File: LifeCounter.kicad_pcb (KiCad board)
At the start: 2 copper layers, 103 x 73 mm, 118 parts, among them J201 USBC, J701 Debug, Q201 2N7002, Q202 BSS84, Q801 2N7002, SW1 RotaryEncoder_Switch_MP, SW2 RotaryEncoder_Switch_MP, SW201 PWR_ON, SW701 RST, U1 74LVC3G14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

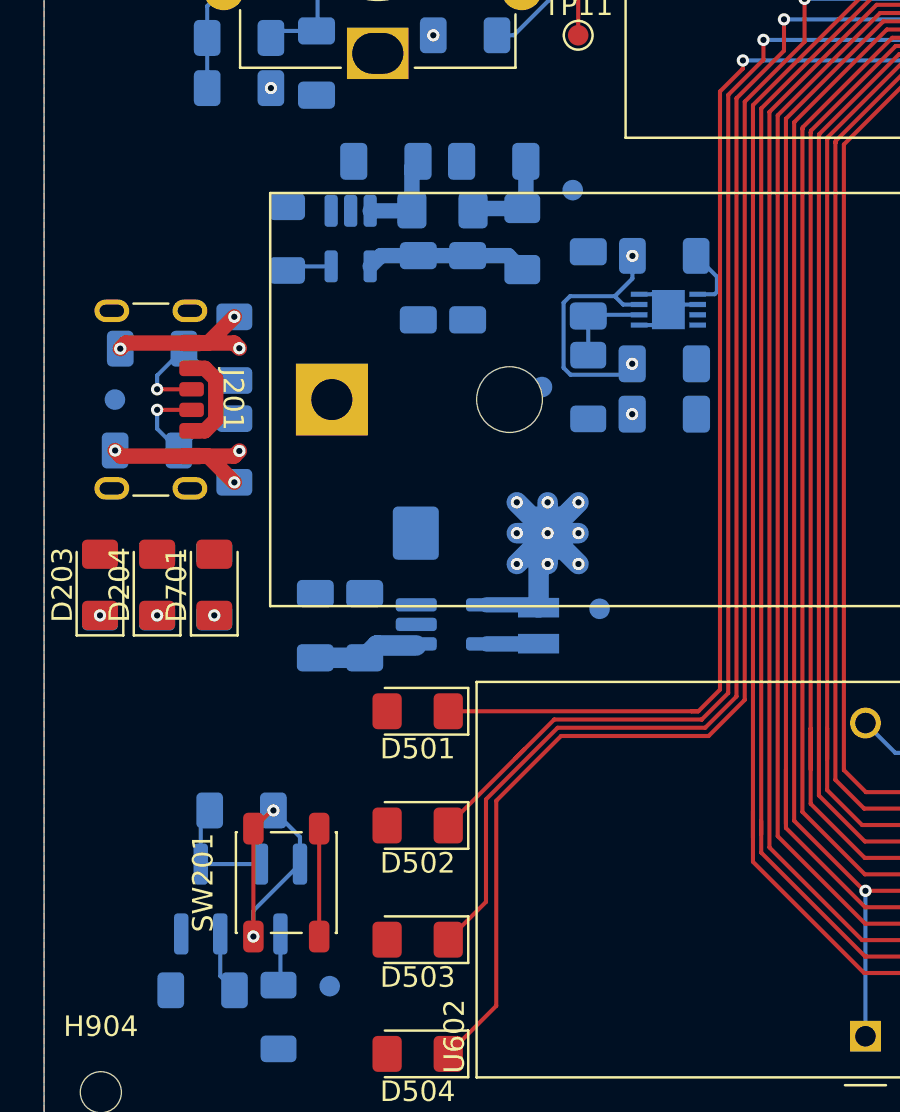
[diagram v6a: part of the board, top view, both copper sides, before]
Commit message: Power routed
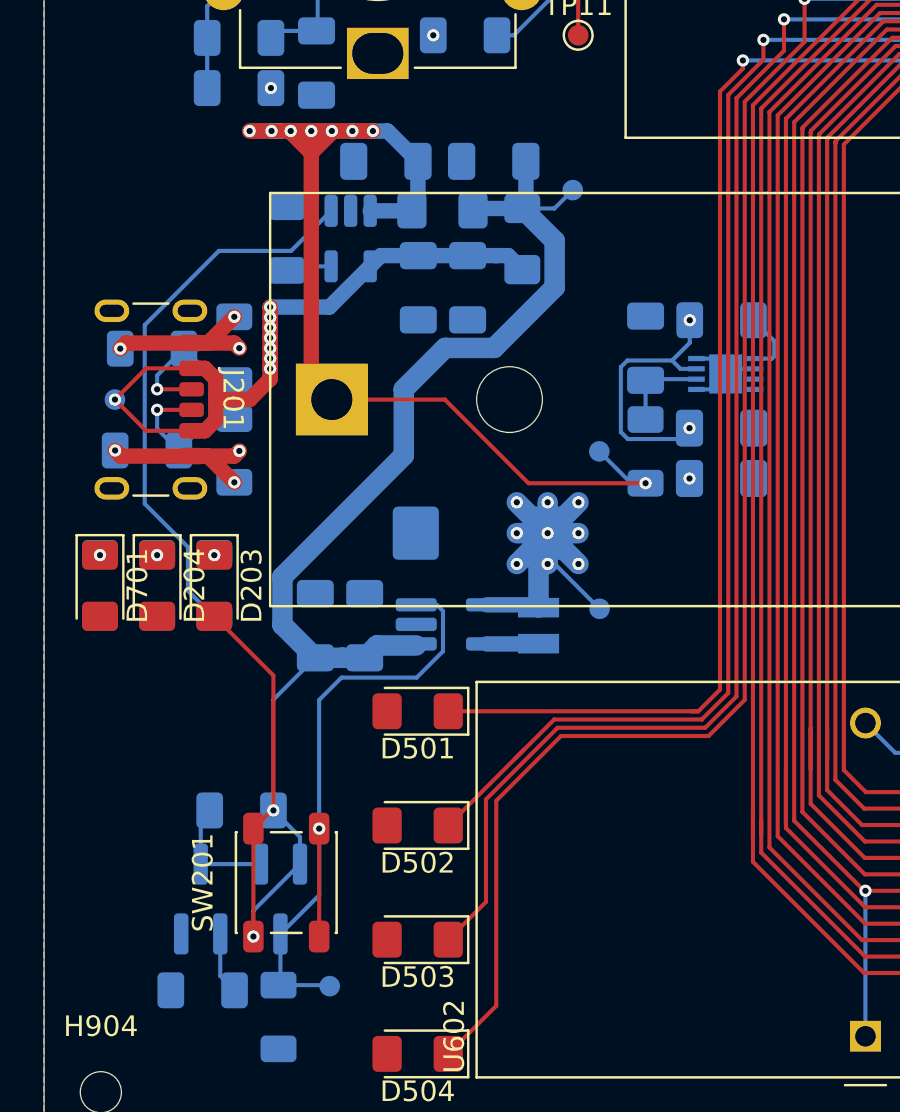
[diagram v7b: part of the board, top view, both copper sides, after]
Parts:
- moved D203 5.56 mm to (-20.2, 116.6), turned to -90 degrees
- moved D701 5.56 mm to (-25.8, 116.6), turned to -90 degrees
- moved R208 5.56 mm to (-20.2, 116.5), turned to -90 degrees
- moved R703 5.56 mm to (-25.8, 116.5), turned to 90 degrees
- moved C201 4.19 mm to (4.46, 111.3)
- moved C202 4.19 mm to (4.46, 108.9)
- moved C203 4.19 mm to (0.76, 105.0)
- moved R203 4.19 mm to (0.76, 110.0)
- moved R204 4.19 mm to (4.46, 103.6)
- moved TP3 4.19 mm to (-1.49, 110.0)
- moved U201 4.19 mm to (4.66, 106.3)
- turned D204 to -90 degrees
- turned R210 to -90 degrees
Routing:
- net /Power/VIN: track 24.2 -> 75.9 mm
- net /Power/VBAT: track 4.55 -> 56.1 mm, vias 0 -> 8
- net Net-(U202-STAT): track 0.00 -> 27.0 mm
- net Net-(Q202-D): track 7.78 -> 32.8 mm, vias 0 -> 1
- net VBUS: track 12.7 -> 36.8 mm, vias 0 -> 8
- net VCC: track 71.9 -> 76.6 mm

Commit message: Routed
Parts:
- TP10, TP11, TP6, TP7, TP8, TP9: moved to B.Cu
- moved TP18 32.9 mm to (15.1, 113.4), turned to 0 degrees
- moved TP17 29.6 mm to (17.6, 113.4), turned to 0 degrees
- moved R701 28.5 mm to (16.6, 110.7), turned to 180 degrees
- moved C703 27.6 mm to (16.8, 105.1), turned to 180 degrees
- moved C702 27.2 mm to (16.8, 107.5), turned to 180 degrees
- moved R702 24.8 mm to (20.2, 114.3), turned to -90 degrees
- moved TP12 23.4 mm to (23.7, 97.8), turned to 0 degrees
- moved TP13 18.8 mm to (24.9, 99.7), turned to 0 degrees
- moved TP15 17.9 mm to (23.4, 112.8), turned to 0 degrees
- moved TP16 14.8 mm to (25.4, 112.7), turned to 0 degrees
- moved U701 11.8 mm to (24.6, 106.3), turned to 0 degrees
- turned TP10 to 0 degrees
- turned TP11 to 180 degrees
- turned TP6 to 0 degrees
- turned TP7 to 180 degrees
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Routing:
- net /Controller/SPI1.Data: track 0.00 -> 71.4 mm, vias 0 -> 4
- net /Controller/~{RST}: track 5.16 -> 75.9 mm, vias 2 -> 4
- net /Controller/SPI1.CLK: track 0.00 -> 69.5 mm, vias 0 -> 4
- net /Controller/PWR_Ctrl: track 3.03 -> 64.5 mm, vias 0 -> 4
- net /Controller/Heartbeat: track 0.00 -> 61.0 mm, vias 0 -> 1
- net /Controller/Debug.SWCLK: track 4.30 -> 54.9 mm, vias 0 -> 2
- net /Controller/Debug.SWDIO: track 4.30 -> 51.6 mm, vias 0 -> 2
- net /Controller/UART1.TX: track 0.00 -> 44.9 mm, vias 0 -> 2
- net /Controller/Encoder2.CLK: track 11.3 -> 53.7 mm, vias 1 -> 4
- net /Buzzer/Buzz: track 2.84 -> 44.7 mm
- net /Controller/UART1.RX: track 0.00 -> 41.9 mm, vias 0 -> 2
- net /Controller/Encoder1.CLK: track 11.1 -> 51.7 mm, vias 1 -> 3
- net /Controller/Encoder2.BTN: track 12.9 -> 53.0 mm, vias 1 -> 4
- net VCC: track 76.6 -> 116.7 mm, vias 32 -> 48
- net /Controller/Encoder1.BTN: track 12.9 -> 52.4 mm, vias 1 -> 3
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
